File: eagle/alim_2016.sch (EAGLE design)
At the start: 74 parts, among them J1 AVR_SPI_PRG_6PTH, U1 3.3V, U4 LM2596S-ADJ, U6 ATMEGA328P_TQFP

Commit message: final version
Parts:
- removed C12: 0.1uF, rcl:C-EUC0805
- removed C8: 1.8nF, rcl:C-EUC0805
- removed SG1: F/CM12P, buzzer:F/CM12P
- removed U$35: 2.2uH, alim:XAL5030
- removed U$38: IRFR8314TRPBF, alim:IRFR8314TRPBF
- removed U$6: TPS54821RHLR, alim:TPS54821RHLR
- removed U6: ATMEGA328P_TQFP, SparkFun-DigitalIC:ATMEGA328P_TQFP
- added C3: 0.1uF, rcl:C-EUC0805
- added C4: 1.8nF, rcl:C-EUC0805
- added L1: 2.2uH, alim:XAL5030
- added U2: TPS54821RHLR, alim:TPS54821RHLR
- added U5: 3.3V, microbuilder:LM1117TO252
- C1: device rcl:CPOL-EUE2.5-7 -> rcl:C-EUC0805
- D1, D2, D3, D4: value (none) -> 5V
- R10, R13: value 1K -> 160
- R11, R3, R6, R8: value 1K -> 200
- R12, R9: value 1K -> 180
- R14: value 1K -> 21K
- R15: value 1K -> 13.7K
- R17: value 1K -> 51.1K
- R18: value 1K -> 10.2K
- R21: value 10K -> 21K
- R5: value 10K -> 13.7K
- U1: value 3.3V -> ATMEGA328P_TQFP; device microbuilder:LM1117TO252 -> SparkFun-DigitalIC:ATMEGA328P_TQFP
- U4: value LM2596S-ADJ -> IRFR8314TRPBF; device alim:LM2596S-ADJ -> alim:IRFR8314TRPBF
- renumbered S1 to BOOT, U$39 to U3
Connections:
- net 12V: now also U2.PVIN_1, U2.PVIN_2, U2.VIN; no longer U$6.PVIN_1, U$6.PVIN_2, U$6.VIN
- net 5.0V: now also C1.1, C3.1, L1.2, U1.VCC@4, U1.VCC@6, U5.IN; no longer C1.+, C12.1, U$35.2, U1.IN, U6.VCC@4, U6.VCC@6
- net BAT12_CUT: now also U4.G; no longer U$38.G
- net COMP: now also U2.COMP; no longer U$6.COMP
- net EN: now also U2.EN; no longer U$6.EN
- net GND: now also C1.2, C3.2, C4.1, U1.GND@3, U1.GND@5, U2.GND_1, U2.GND_2, U2.PAD, U4.D, U5.ADJ; no longer C1.-, C12.2, C8.1, U$38.D, U$6.GND_1, U$6.GND_2, U$6.PAD, U1.ADJ, U4.GND, U4.GND_2, U6.GND@3, U6.GND@5
- net N$1: now also U5.OUT; no longer U1.OUT
- net N$11: now also U1.PD4(XCK/T0); no longer U6.PD4(XCK/T0)
- net N$13: now also U4.S; no longer U$38.S
- net N$14: now also U1.PC1(ADC1); no longer U6.PC1(ADC1)
- net N$2: now also U1.PB5(SCK); no longer U6.PB5(SCK)
- net N$21: now also U1.PC2(ADC2); no longer U6.PC2(ADC2)
- net N$22: now also U1.PC0(ADC0); no longer U6.PC0(ADC0)
- net N$23: now also U1.ADC7; no longer U6.ADC7
- net N$24: now also U1.PD3(INT1); no longer U6.PD3(INT1)
- net N$25: now also U1.PD2(INT0); no longer U6.PD2(INT0)
- net N$26: now also U1.PD1(TXD); no longer U6.PD1(TXD)
- net N$27: now also U1.ADC6; no longer U6.ADC6
- net N$28: now also U1.PC4(ADC4/SDA); no longer U6.PC4(ADC4/SDA)
- net N$3: now also U1.PB4(MISO); no longer U6.PB4(MISO)
- net N$31: now also U2.BOOT; no longer U$6.BOOT
- net N$35: now also U2.PWRGD; no longer U$6.PWRGD
- net N$4: now also U1.PB3(MOSI/OC2); no longer U6.PB3(MOSI/OC2)
- net N$6: now also U1.PD5(T1); no longer U6.PD5(T1)
- net PH: now also L1.1, U2.PH_1, U2.PH_2; no longer U$35.1, U$6.PH_1, U$6.PH_2
- net RESET: now also U1.PC6(/RESET); no longer U6.PC6(/RESET)
- net RTCLK: now also U2.RT/CLK; no longer U$6.RT/CLK
- net SSTR: now also C4.2, U2.SS/TR; no longer C8.2, U$6.SS/TR
- net VSENSE: now also U2.VSENSE; no longer U$6.VSENSE
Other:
- moved on the sheet: 3.3V-1, 3.3V-2, 5V_1-1, 5V_1-2, 5V_2-1, 5V_2-2, 5V_3-1, 5V_3-2, 5V_4-1, 5V_4-2, 5V_5-1, 5V_5-2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

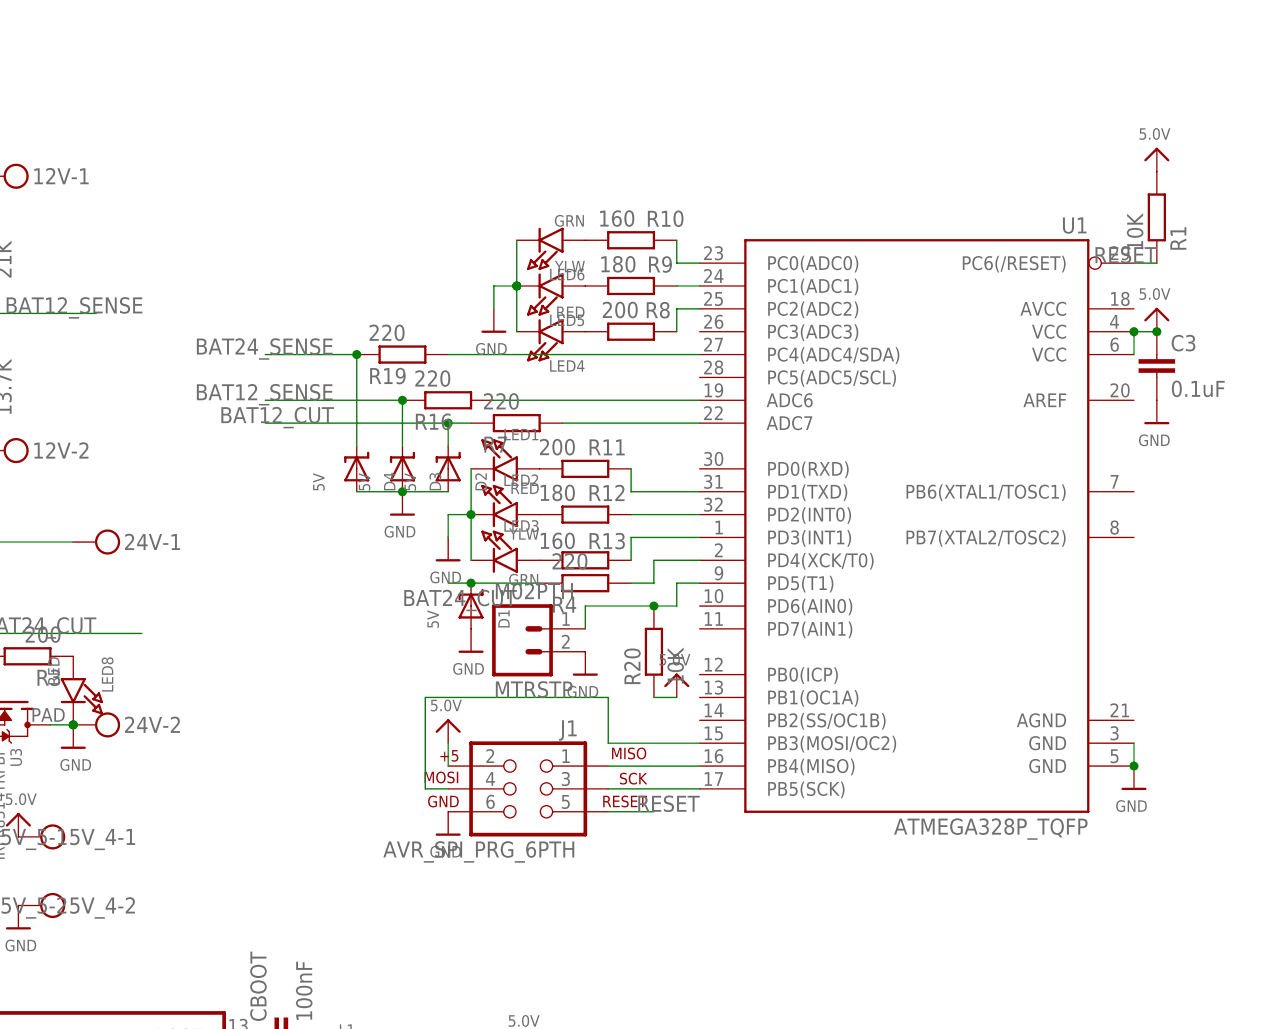
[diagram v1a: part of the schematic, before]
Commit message: fix routing error: ADC7 cannot be a GPIO
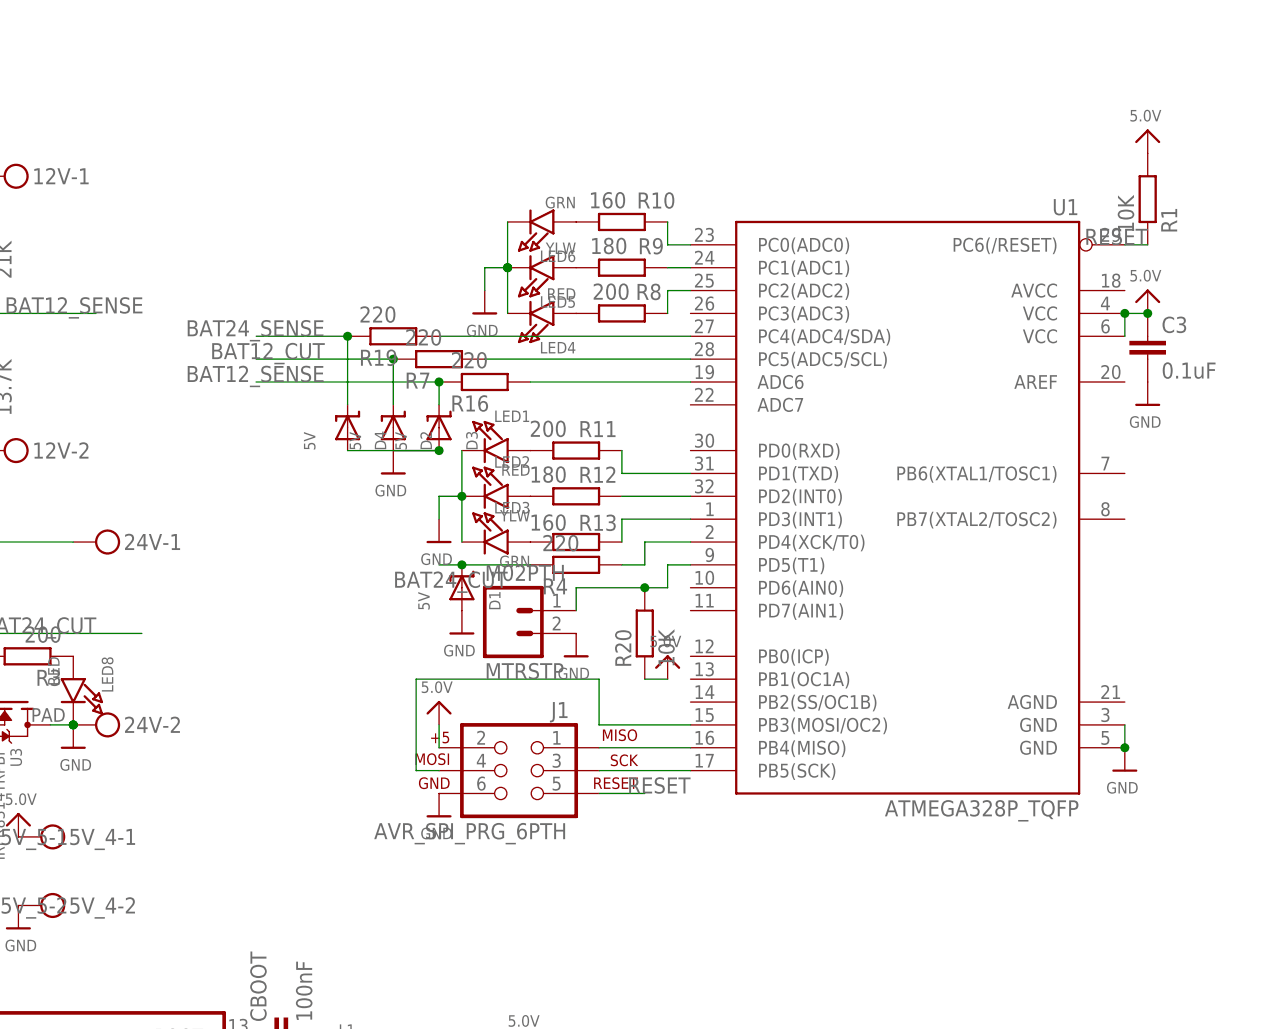
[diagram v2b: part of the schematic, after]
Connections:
- net N$2 renamed SCK
- net N$3 renamed MISO
- net N$4 renamed MOSI
- net N$23: now also U1.PC5(ADC5/SCL); no longer U1.ADC7
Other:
- moved on the sheet: C3, D1, D2, D3, D4, J1, LED1, LED2, LED3, LED4, LED5, LED6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
